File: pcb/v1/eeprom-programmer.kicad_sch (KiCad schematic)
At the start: 62 parts, among them J1 USB_C_Receptacle_USB2.0_16P, J2 Conn_01x04, J3 Conn_01x20, J4 Conn_01x20, SW1 SW_Push_Dual, SW2 SW_Push_Dual, SW3 SW_Push_Dual, U1 W25Q32JVSS, U2 USBLC6-2SC6, U3 RP2040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

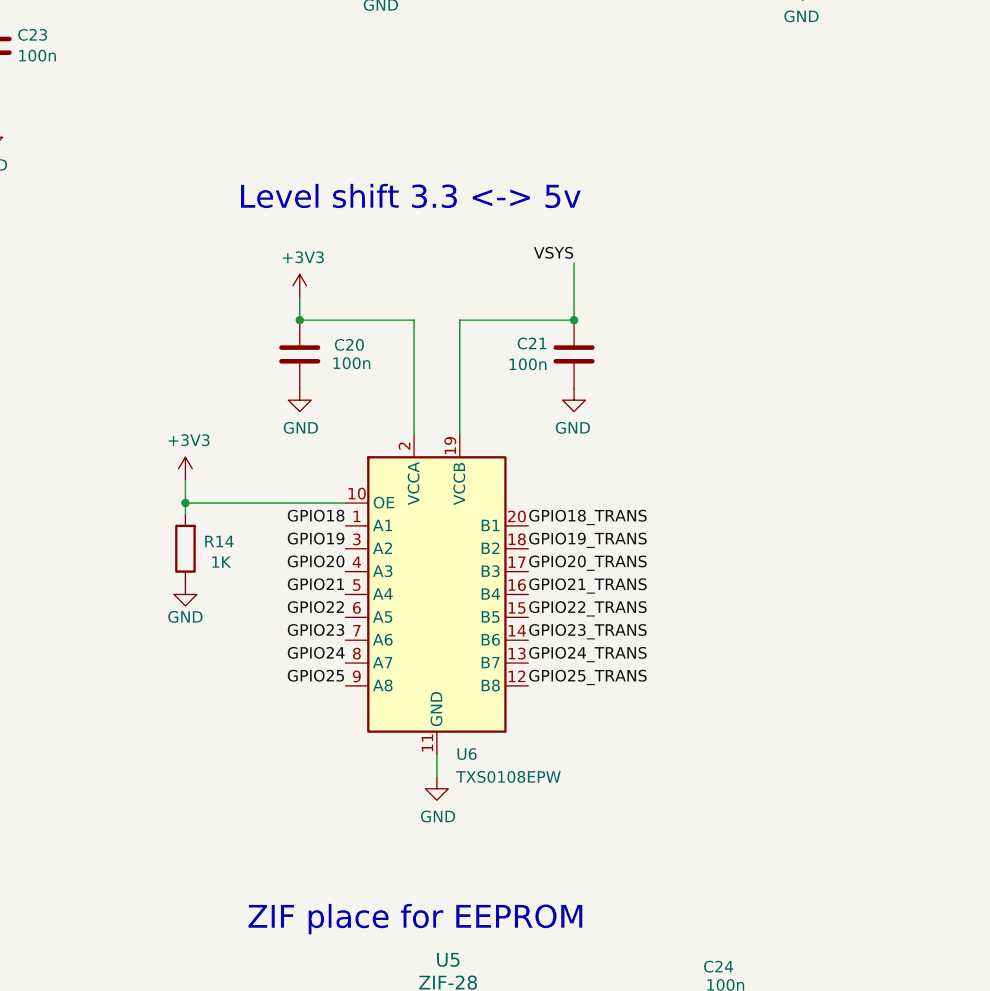
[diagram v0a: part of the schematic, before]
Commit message: fix 2 mixed up labels; update output files; add pcb with rounded labels
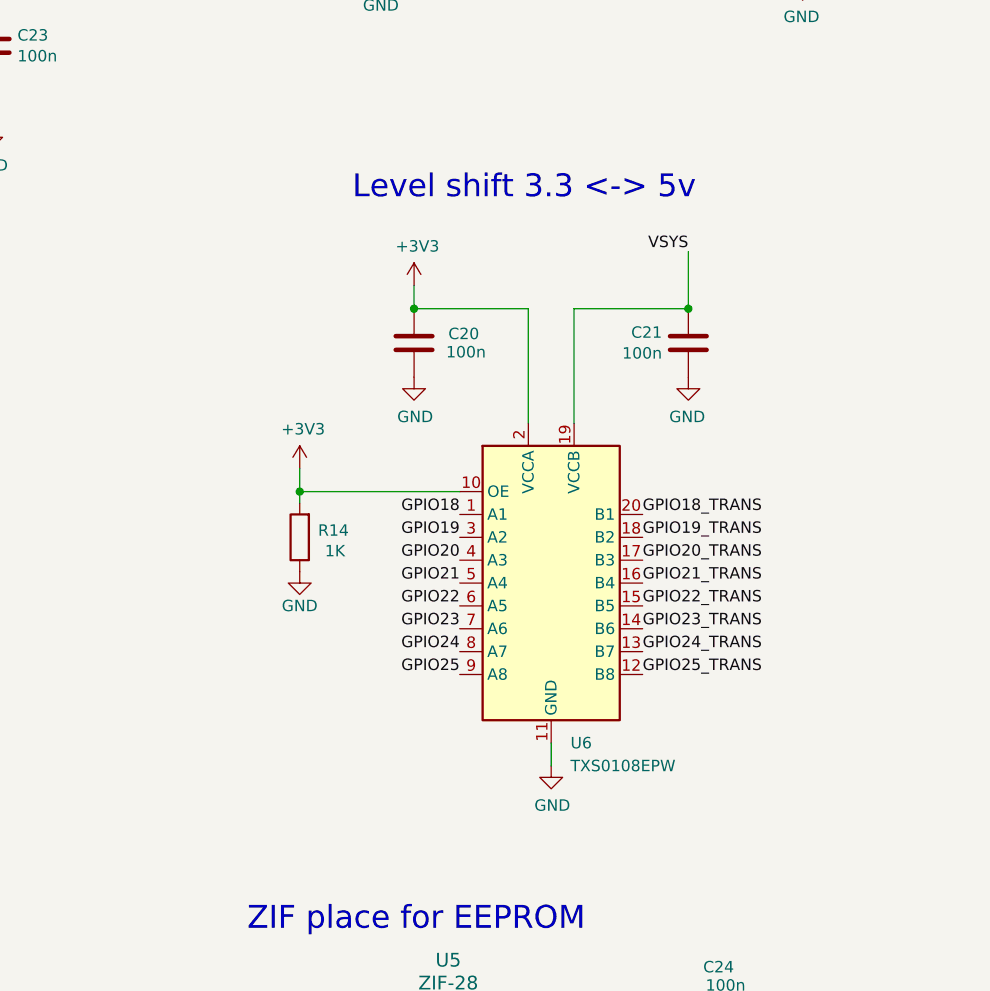
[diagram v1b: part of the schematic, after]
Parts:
- C12, C16, C19, C22, C6: Buy Link https://imrad.com.ua/ua/cl10a106mo8nqnc-2 -> https://imrad.com.ua/ua/cl10a106kp8nnnc-6
- U4: Buy Link https://imrad.com.ua/ua/ncp1117st33t3g-8 -> https://www.rcscomponents.kiev.ua/product/ncp1117st33t3g_26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
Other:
- moved on the sheet: C20, C21, R14, U6
